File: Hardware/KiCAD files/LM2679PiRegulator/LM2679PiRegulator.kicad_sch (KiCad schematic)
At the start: 14 parts, among them J2 Conn_01x03_Pin, U1 LM2679SX-5V

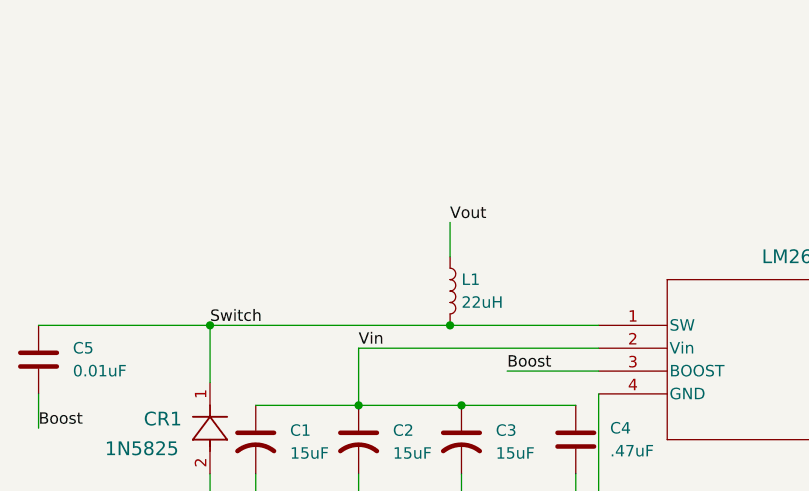
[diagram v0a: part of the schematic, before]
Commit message: general progress and adjustments
new footprint for pi reg inductor, var reg checked concurred with current part and value. re footprinted motor driver. started swapping head. adjusted some device footprints.
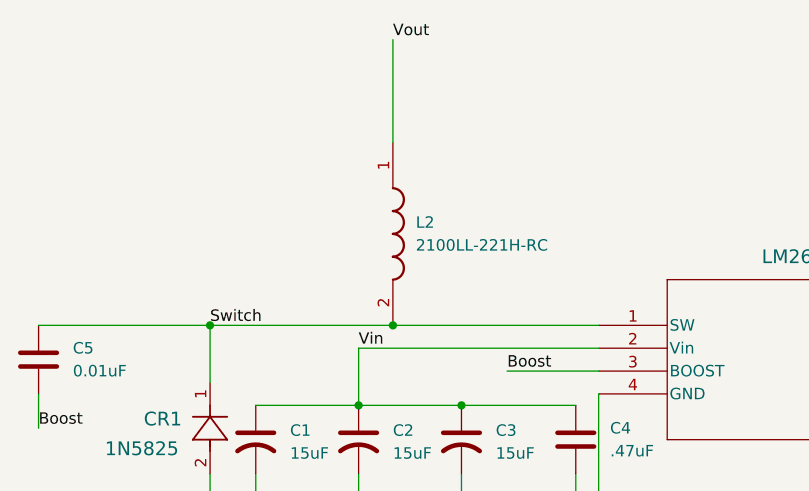
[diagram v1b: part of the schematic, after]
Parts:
- removed L1: 22uH, Inductor_SMD:L_1206_3216Metric_Pad1.22x1.90mm_HandSolder, symbol Device:L
- added L2: 2100LL-221H-RC, 2100LL221HRC, symbol 2100LL-221H-RC:2100LL-221H-RC
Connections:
- net Switch: now also L2.2
- net Vout: now also L2.1

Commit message: V2 mainboard
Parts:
- L2: value 2100LL-221H-RC -> 22uh
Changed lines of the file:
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@@
 			)
 		)
-		(property "Value" "2100LL-221H-RC"
+		(property "Value" "22uh"
 			(at 69.85 57.1499 90)
 			(show_name no)
